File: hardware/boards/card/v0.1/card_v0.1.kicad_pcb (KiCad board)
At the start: 6 copper layers, 67.6 x 25.4 mm, 63 parts, among them IC1 IS42S16160J-7BLI, IC2 IS42S16160J-7BLI, J1 SODIMM-200, J2 USB_HOST, J3 USB_DEVICE, J4 SD_CARD, J5 DEBUG, J6 SPI, J7 UART4, J8 Conn_01x16_Pin, J9 AUDIO_IN, U1 CS42528K-CQZ, U2 STM32H747XIHx, U3 NJM4580E-TE1, U4 NJM4580E-TE1, Y1 Crystal, Y2 Crystal

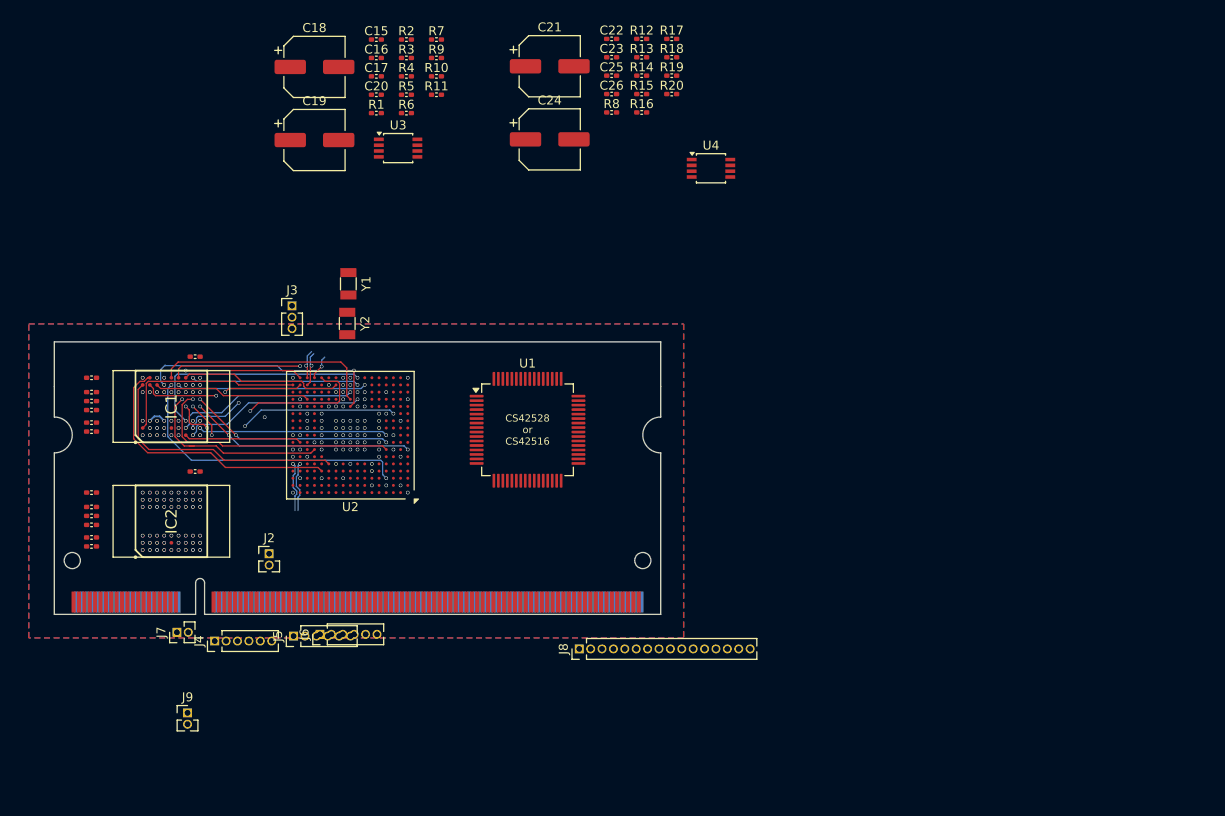
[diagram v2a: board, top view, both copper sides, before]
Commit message: boards/card: route audio input channels and 4 output channel buffers
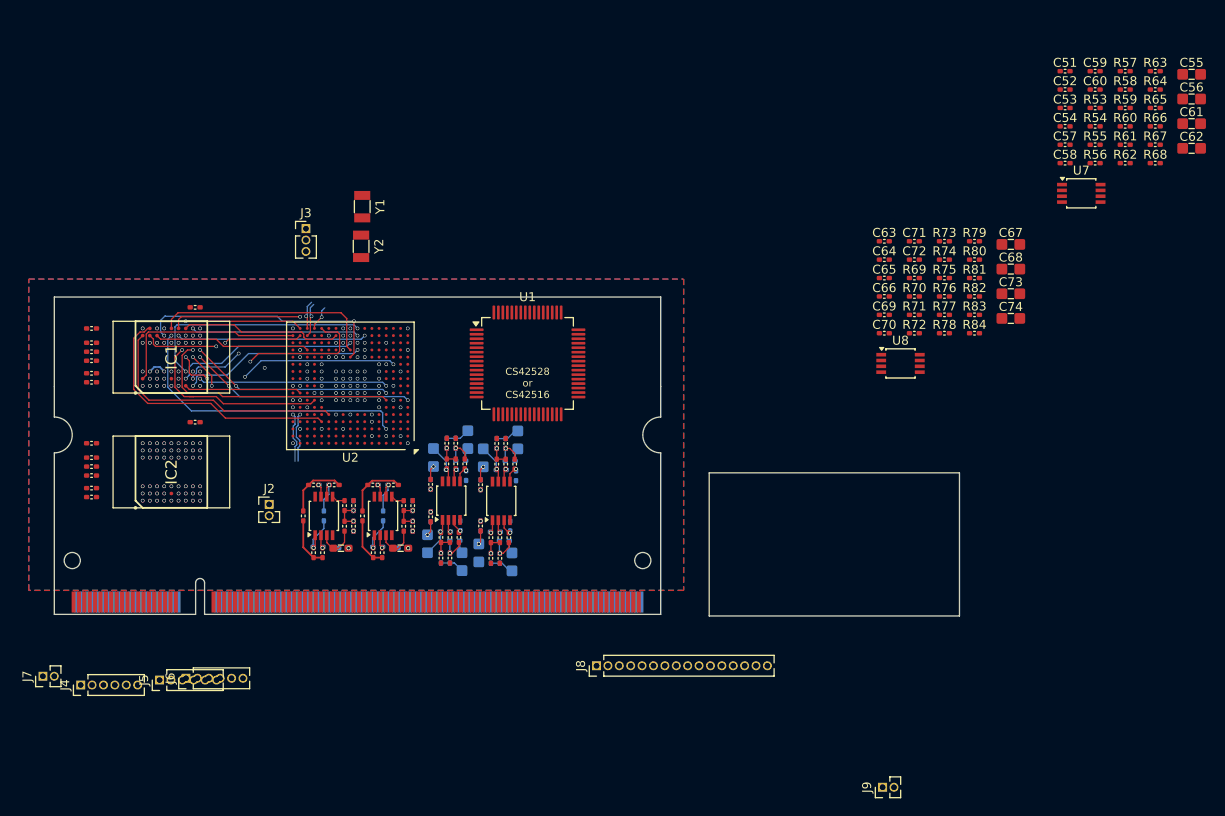
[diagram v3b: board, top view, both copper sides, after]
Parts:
- added C27: 2n2 FILM, rhais_rcl.pretty-main:C0603, F.Cu at (88.5, 69.0)
- added C28: 2n2 FILM, rhais_rcl.pretty-main:C0603, F.Cu at (81.8, 69.0)
- added C29: 4.7uF X7R, rhais_rcl.pretty-main:C0402, B.Cu at (83.2, 66.5)
- added C30: 47uF X5R, rhais_rcl.pretty-main:C0805, B.Cu at (95.3, 70.5)
- added C31: 1n2 C0G, rhais_rcl.pretty-main:C0402, B.Cu at (95.1, 66.5)
- added C32: 47uF X5R, rhais_rcl.pretty-main:C0805, B.Cu at (91.5, 68.5)
- added C33: 1n8 C0G, rhais_rcl.pretty-main:C0402, B.Cu at (93.6, 57.3)
- added C34: 5n8 C0G, rhais_rcl.pretty-main:C0402, B.Cu at (94.6, 57.3)
- added C35: 47uF X5R, rhais_rcl.pretty-main:C0805, B.Cu at (96.0, 56.9)
- added C36: 1n2 C0G, rhais_rcl.pretty-main:C0402, B.Cu at (95.8, 60.9)
- added C37: 390pF C0G, rhais_rcl.pretty-main:C0402, B.Cu at (94.1, 60.2)
- added C38: 47uF X5R, rhais_rcl.pretty-main:C0805, B.Cu at (92.1, 58.9)
- added C39: 1n8 C0G, rhais_rcl.pretty-main:C0402, B.Cu at (98.5, 70.1)
- added C40: 5n8 C0G, rhais_rcl.pretty-main:C0402, B.Cu at (99.5, 70.1)
- added C41: 1n8 C0G, rhais_rcl.pretty-main:C0402, B.Cu at (99.2, 57.3)
- added C42: 5n8 C0G, rhais_rcl.pretty-main:C0402, B.Cu at (100.2, 57.3)
- added C43: 47uF X5R, rhais_rcl.pretty-main:C0805, B.Cu at (100.9, 70.5)
- added C44: 47uF X5R, rhais_rcl.pretty-main:C0805, B.Cu at (101.5, 56.9)
- added C45: 1n2 C0G, rhais_rcl.pretty-main:C0402, B.Cu at (100.7, 66.5)
- added C46: 1n2 C0G, rhais_rcl.pretty-main:C0402, B.Cu at (101.3, 60.9)
- added C47: 390pF C0G, rhais_rcl.pretty-main:C0402, B.Cu at (99.0, 67.2)
- added C48: 390pF C0G, rhais_rcl.pretty-main:C0402, B.Cu at (99.7, 60.3)
- added C49: 47uF X5R, rhais_rcl.pretty-main:C0805, B.Cu at (97.2, 69.5)
- added C50: 47uF X5R, rhais_rcl.pretty-main:C0805, B.Cu at (97.7, 58.9)
- added C51: 1n8 C0G, rhais_rcl.pretty-main:C0402, F.Cu at (162.5, 15.8)
- added C52: 5n8 C0G, rhais_rcl.pretty-main:C0402, F.Cu at (162.5, 17.9)
- added C53: 1n8 C0G, rhais_rcl.pretty-main:C0402, F.Cu at (162.5, 19.9)
- added C54: 5n8 C0G, rhais_rcl.pretty-main:C0402, F.Cu at (162.5, 22.0)
- added C55: 47uF X5R, rhais_rcl.pretty-main:C0805, F.Cu at (176.6, 16.2)
- added C56: 47uF X5R, rhais_rcl.pretty-main:C0805, F.Cu at (176.6, 18.9)
- added C57: 1n2 C0G, rhais_rcl.pretty-main:C0402, F.Cu at (162.5, 24.0)
- added C58: 1n2 C0G, rhais_rcl.pretty-main:C0402, F.Cu at (162.5, 26.1)
- added C59: 390pF C0G, rhais_rcl.pretty-main:C0402, F.Cu at (165.9, 15.8)
- added C60: 390pF C0G, rhais_rcl.pretty-main:C0402, F.Cu at (165.9, 17.9)
- added C61: 47uF X5R, rhais_rcl.pretty-main:C0805, F.Cu at (176.6, 21.7)
- added C62: 47uF X5R, rhais_rcl.pretty-main:C0805, F.Cu at (176.6, 24.4)
- added C63: 1n8 C0G, rhais_rcl.pretty-main:C0402, F.Cu at (142.4, 34.8)
- added C64: 5n8 C0G, rhais_rcl.pretty-main:C0402, F.Cu at (142.4, 36.8)
- added C65: 1n8 C0G, rhais_rcl.pretty-main:C0402, F.Cu at (142.4, 38.9)
- added C66: 5n8 C0G, rhais_rcl.pretty-main:C0402, F.Cu at (142.4, 40.9)
- added C67: 47uF X5R, rhais_rcl.pretty-main:C0805, F.Cu at (156.5, 35.1)
- added C68: 47uF X5R, rhais_rcl.pretty-main:C0805, F.Cu at (156.5, 37.9)
- added C69: 1n2 C0G, rhais_rcl.pretty-main:C0402, F.Cu at (142.4, 43.0)
- added C70: 1n2 C0G, rhais_rcl.pretty-main:C0402, F.Cu at (142.4, 45.0)
- added C71: 390pF C0G, rhais_rcl.pretty-main:C0402, F.Cu at (145.7, 34.8)
- added C72: 390pF C0G, rhais_rcl.pretty-main:C0402, F.Cu at (145.7, 36.8)
- added C73: 47uF X5R, rhais_rcl.pretty-main:C0805, F.Cu at (156.5, 40.6)
- added C74: 47uF X5R, rhais_rcl.pretty-main:C0805, F.Cu at (156.5, 43.4)
- added R21: 2k94, rhais_rcl.pretty-main:R0402, F.Cu at (94.0, 67.8)
- added R22: 5k49, rhais_rcl.pretty-main:R0402, F.Cu at (93.0, 70.1)
- added R23: 1k65, rhais_rcl.pretty-main:R0402, F.Cu at (94.0, 70.1)
- added R24: 887R, rhais_rcl.pretty-main:R0402, F.Cu at (95.0, 67.8)
- added R25: 6k19, rhais_rcl.pretty-main:R0402, F.Cu at (93.0, 67.8)
- added R26: 1k87, rhais_rcl.pretty-main:R0402, B.Cu at (94.5, 68.2)
- added R27: 1k, rhais_rcl.pretty-main:R0402, F.Cu at (91.8, 65.5)
- added R28: 47k5, rhais_rcl.pretty-main:R0402, B.Cu at (91.8, 65.5)
- added R29: 5k49, rhais_rcl.pretty-main:R0402, F.Cu at (93.6, 57.3)
- added R30: 1k65, rhais_rcl.pretty-main:R0402, F.Cu at (94.6, 57.3)
- added R31: 6k19, rhais_rcl.pretty-main:R0402, F.Cu at (93.6, 59.6)
- added R32: 2k94, rhais_rcl.pretty-main:R0402, F.Cu at (94.6, 59.6)
- added R33: 887R, rhais_rcl.pretty-main:R0402, F.Cu at (95.6, 59.6)
- added R34: 1k87, rhais_rcl.pretty-main:R0402, B.Cu at (95.2, 59.2)
- added R35: 1k, rhais_rcl.pretty-main:R0402, F.Cu at (91.8, 61.9)
- added R36: 47k5, rhais_rcl.pretty-main:R0402, B.Cu at (91.8, 61.9)
- added R37: 5k49, rhais_rcl.pretty-main:R0402, F.Cu at (98.5, 70.1)
- added R38: 1k65, rhais_rcl.pretty-main:R0402, F.Cu at (99.5, 70.1)
- added R39: 5k49, rhais_rcl.pretty-main:R0402, F.Cu at (99.2, 57.3)
- added R40: 1k65, rhais_rcl.pretty-main:R0402, F.Cu at (100.2, 57.3)
- added R41: 6k19, rhais_rcl.pretty-main:R0402, F.Cu at (98.5, 67.8)
- added R42: 2k94, rhais_rcl.pretty-main:R0402, F.Cu at (99.5, 67.8)
- added R43: 887R, rhais_rcl.pretty-main:R0402, F.Cu at (100.5, 67.8)
- added R44: 1k87, rhais_rcl.pretty-main:R0402, B.Cu at (100.0, 68.2)
- added R45: 6k19, rhais_rcl.pretty-main:R0402, F.Cu at (99.2, 59.6)
- added R46: 2k94, rhais_rcl.pretty-main:R0402, F.Cu at (100.2, 59.6)
- added R47: 887R, rhais_rcl.pretty-main:R0402, F.Cu at (101.2, 59.6)
- added R48: 1k87, rhais_rcl.pretty-main:R0402, B.Cu at (100.7, 59.3)
- added R49: 1k, rhais_rcl.pretty-main:R0402, F.Cu at (97.4, 66.5)
- added R50: 1k, rhais_rcl.pretty-main:R0402, F.Cu at (97.4, 61.9)
- added R51: 47k5, rhais_rcl.pretty-main:R0402, B.Cu at (97.4, 66.5)
- added R52: 47k5, rhais_rcl.pretty-main:R0402, B.Cu at (97.4, 61.9)
- added R53: 5k49, rhais_rcl.pretty-main:R0402, F.Cu at (165.9, 19.9)
- added R54: 1k65, rhais_rcl.pretty-main:R0402, F.Cu at (165.9, 22.0)
- added R55: 5k49, rhais_rcl.pretty-main:R0402, F.Cu at (165.9, 24.0)
- added R56: 1k65, rhais_rcl.pretty-main:R0402, F.Cu at (165.9, 26.1)
- added R57: 6k19, rhais_rcl.pretty-main:R0402, F.Cu at (169.2, 15.8)
- added R58: 2k94, rhais_rcl.pretty-main:R0402, F.Cu at (169.2, 17.9)
- added R59: 887R, rhais_rcl.pretty-main:R0402, F.Cu at (169.2, 19.9)
- added R60: 1k87, rhais_rcl.pretty-main:R0402, F.Cu at (169.2, 22.0)
- added R61: 6k19, rhais_rcl.pretty-main:R0402, F.Cu at (169.2, 24.0)
- added R62: 2k94, rhais_rcl.pretty-main:R0402, F.Cu at (169.2, 26.1)
- added R63: 887R, rhais_rcl.pretty-main:R0402, F.Cu at (172.6, 15.8)
- added R64: 1k87, rhais_rcl.pretty-main:R0402, F.Cu at (172.6, 17.9)
- added R65: 1k, rhais_rcl.pretty-main:R0402, F.Cu at (172.6, 19.9)
- added R66: 1k, rhais_rcl.pretty-main:R0402, F.Cu at (172.6, 22.0)
- added R67: 47k5, rhais_rcl.pretty-main:R0402, F.Cu at (172.6, 24.0)
- added R68: 47k5, rhais_rcl.pretty-main:R0402, F.Cu at (172.6, 26.1)
- added R69: 5k49, rhais_rcl.pretty-main:R0402, F.Cu at (145.7, 38.9)
- added R70: 1k65, rhais_rcl.pretty-main:R0402, F.Cu at (145.7, 40.9)
- added R71: 5k49, rhais_rcl.pretty-main:R0402, F.Cu at (145.7, 43.0)
- added R72: 1k65, rhais_rcl.pretty-main:R0402, F.Cu at (145.7, 45.0)
- added R73: 6k19, rhais_rcl.pretty-main:R0402, F.Cu at (149.1, 34.8)
- added R74: 2k94, rhais_rcl.pretty-main:R0402, F.Cu at (149.1, 36.8)
- added R75: 887R, rhais_rcl.pretty-main:R0402, F.Cu at (149.1, 38.9)
- added R76: 1k87, rhais_rcl.pretty-main:R0402, F.Cu at (149.1, 40.9)
- added R77: 6k19, rhais_rcl.pretty-main:R0402, F.Cu at (149.1, 43.0)
- added R78: 2k94, rhais_rcl.pretty-main:R0402, F.Cu at (149.1, 45.0)
- added R79: 887R, rhais_rcl.pretty-main:R0402, F.Cu at (152.4, 34.8)
- added R80: 1k87, rhais_rcl.pretty-main:R0402, F.Cu at (152.4, 36.8)
- added R81: 1k, rhais_rcl.pretty-main:R0402, F.Cu at (152.4, 38.9)
- added R82: 1k, rhais_rcl.pretty-main:R0402, F.Cu at (152.4, 40.9)
- added R83: 47k5, rhais_rcl.pretty-main:R0402, F.Cu at (152.4, 43.0)
- added R84: 47k5, rhais_rcl.pretty-main:R0402, F.Cu at (152.4, 45.0)
- added U5: NJM4580E-TE1, Package_SO:TSSOP-8_3x3mm_P0.65mm, F.Cu at (94.1, 63.7)
- added U6: NJM4580E-TE1, Package_SO:TSSOP-8_3x3mm_P0.65mm, F.Cu at (99.7, 63.7)
- added U7: NJM4580E-TE1, Package_SO:TSSOP-8_3x3mm_P0.65mm, F.Cu at (164.3, 29.4)
- added U8: NJM4580E-TE1, Package_SO:TSSOP-8_3x3mm_P0.65mm, F.Cu at (144.2, 48.4)
- C15, C26: value 2700pF C0G -> 2n7 C0G
- C16, C17, C20, C22, C23, C25, R17, R3: moved to B.Cu
- C18: value 100uF ELEC -> 1n8 C0G; footprint Capacitor_SMD:CP_Elec_6.3x5.7 -> rhais_rcl.pretty-main:C0402; moved to B.Cu
- C19: value 100uF ELEC -> 5n8 C0G; footprint Capacitor_SMD:CP_Elec_6.3x5.7 -> rhais_rcl.pretty-main:C0402; moved to B.Cu
- C21: value 100uF ELEC -> 4.7uF X7R; footprint Capacitor_SMD:CP_Elec_6.3x5.7 -> rhais_rcl.pretty-main:C0402; moved to B.Cu
- C24: value 100uF ELEC -> 390pF C0G; footprint Capacitor_SMD:CP_Elec_6.3x5.7 -> rhais_rcl.pretty-main:C0402; moved to B.Cu
- R11, R12: value 100k -> 10k; moved to B.Cu
- moved J9 77.9 mm to (142.2, 95.7), turned to 90 degrees
- moved R18 68.1 mm to (78.8, 69.5), turned to -90 degrees
- moved R17 65.8 mm to (79.9, 65.4), turned to 90 degrees
- moved R12 65.8 mm to (82.1, 69.0), turned to 180 degrees
- moved C23 63.6 mm to (79.2, 68.8), turned to 180 degrees
- moved R15 62.3 mm to (79.8, 69.5), turned to -90 degrees
- moved R14 59.6 mm to (83.2, 66.5), turned to -90 degrees
- moved C22 59.5 mm to (83.2, 64.2), turned to 90 degrees
- moved R13 59.4 mm to (83.2, 64.2), turned to -90 degrees
- moved R19 59.1 mm to (81.0, 62.0)
- moved R20 59.1 mm to (78.8, 62.0), turned to 180 degrees
- moved C26 58.2 mm to (77.6, 65.4), turned to 90 degrees
- moved U4 58.0 mm to (79.9, 65.4), turned to 90 degrees
- moved C18 56.5 mm to (93.0, 70.1), turned to 90 degrees
- moved C25 55.8 mm to (79.9, 62.0), turned to 180 degrees
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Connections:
- C16 pad 1: Net-(U3B-+) -> Net-(U3B--)
- C17 pad 1: Net-(U3A-+) -> Net-(U3A--)
- C18 pad 1: Net-(U3A-+) -> GND
- C18 pad 2: /IN_L -> Net-(C18-Pad2)
- C19 pad 1: Net-(C19-Pad1) -> GND
- C19 pad 2: GND -> Net-(C19-Pad2)
- C20 pad 1: Net-(C19-Pad1) -> Net-(C20-Pad1)
- C21 pad 1: Net-(U4A-+) -> Net-(C20-Pad1)
- C21 pad 2: /IN_R -> GND
- C23 pad 1: Net-(U4A-+) -> Net-(U4A--)
- C24 pad 1: Net-(C22-Pad1) -> Net-(U5A--)
- C24 pad 2: GND -> Net-(C24-Pad2)
- C25 pad 1: Net-(U4B-+) -> Net-(U4B--)
- J8 pad 1: Net-(J8-Pin_1) -> /OUT_B4
- J8 pad 10: Net-(J8-Pin_10) -> /OUT_B1
- J8 pad 11: Net-(J8-Pin_11) -> /OUT_A1
- J8 pad 12: Net-(J8-Pin_12) -> unconnected-(J8-Pin_12-Pad12)
- J8 pad 13: Net-(J8-Pin_13) -> unconnected-(J8-Pin_13-Pad13)
- J8 pad 14: Net-(J8-Pin_14) -> unconnected-(J8-Pin_14-Pad14)
- J8 pad 15: Net-(J8-Pin_15) -> unconnected-(J8-Pin_15-Pad15)
- J8 pad 16: Net-(J8-Pin_16) -> unconnected-(J8-Pin_16-Pad16)
- J8 pad 2: Net-(J8-Pin_2) -> /OUT_A4
- J8 pad 3: Net-(J8-Pin_3) -> unconnected-(J8-Pin_3-Pad3)
- J8 pad 4: Net-(J8-Pin_4) -> /OUT_B3
- J8 pad 5: Net-(J8-Pin_5) -> /OUT_A3
- J8 pad 6: Net-(J8-Pin_6) -> unconnected-(J8-Pin_6-Pad6)
- J8 pad 7: Net-(J8-Pin_7) -> /OUT_B2
- J8 pad 8: Net-(J8-Pin_8) -> /OUT_A2
- J8 pad 9: Net-(J8-Pin_9) -> unconnected-(J8-Pin_9-Pad9)
- R10 pad 1: Net-(C19-Pad1) -> Net-(C20-Pad1)
- R15 pad 1: Net-(U4A-+) -> Net-(U4A--)
- R16 pad 2: Net-(U4B--) -> Net-(U4B-+)
- R17 pad 2: Net-(U4B-+) -> Net-(U4B--)
- R19 pad 1: Net-(U4B-+) -> Net-(U4B--)
- R2 pad 1: Net-(U3B-+) -> Net-(U3B--)
- R3 pad 2: Net-(U3B-+) -> Net-(U3B--)
- R5 pad 1: Net-(U3A-+) -> Net-(U3A--)
- R6 pad 1: Net-(C19-Pad1) -> Net-(C20-Pad1)
- R6 pad 2: Net-(U3B--) -> Net-(U3B-+)
- R7 pad 1: Net-(C19-Pad1) -> Net-(C20-Pad1)
- R7 pad 2: Net-(U3A--) -> Net-(U3A-+)
- R8 pad 2: Net-(U4A--) -> Net-(U4A-+)
- R9 pad 2: Net-(C19-Pad1) -> Net-(C20-Pad1)
- U1 pad 20: Net-(J8-Pin_1) -> /AOUTB4-
- U1 pad 21: Net-(J8-Pin_2) -> /AOUTB4+
- U1 pad 22: Net-(J8-Pin_4) -> /AOUTA4+
- U1 pad 23: Net-(J8-Pin_3) -> /AOUTA4-
- U1 pad 26: Net-(J8-Pin_5) -> /AOUTB3-
- U1 pad 27: Net-(J8-Pin_6) -> /AOUTB3+
- U1 pad 28: Net-(J8-Pin_8) -> /AOUTA3+
- U1 pad 29: Net-(J8-Pin_7) -> /AOUTA3-
- U1 pad 30: Net-(J8-Pin_9) -> /AOUTB2-
- U1 pad 31: Net-(J8-Pin_10) -> /AOUTB2+
- U1 pad 32: Net-(J8-Pin_12) -> /AOUTA2+
- U1 pad 33: Net-(J8-Pin_11) -> /AOUTA2-
- U1 pad 34: Net-(J8-Pin_13) -> /AOUTB1-
- U1 pad 35: Net-(J8-Pin_14) -> /AOUTB1+
- U1 pad 36: Net-(J8-Pin_16) -> /AOUTA1+
- U1 pad 37: Net-(J8-Pin_15) -> /AOUTA1-
- U3 pad 4: unconnected-(U3C-V--Pad4) -> GND
- U3 pad 8: unconnected-(U3C-V+-Pad8) -> +5V
- U4 pad 4: (no net) -> +5V
- U4 pad 8: (no net) -> GND
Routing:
- net GND: track 0.00 -> 11.1 mm, vias 61 -> 63
- net /AINR-: track 0.00 -> 6.96 mm
- net /AINL-: track 0.00 -> 6.94 mm
- net /AINL+: track 0.00 -> 5.60 mm
- net /AINR+: track 0.00 -> 5.58 mm
- net Net-(C23-Pad2): track 0.00 -> 4.87 mm, vias 0 -> 1
- net Net-(C17-Pad2): track 0.00 -> 4.83 mm, vias 0 -> 1
- net Net-(U3A-+): track 0.00 -> 4.64 mm
- net Net-(U4A-+): track 0.00 -> 4.62 mm
- net Net-(U4B--): track 0.00 -> 4.54 mm, vias 0 -> 1
- net Net-(U3B--): track 0.00 -> 4.54 mm, vias 0 -> 1
- net Net-(C37-Pad2): track 0.00 -> 4.42 mm, vias 0 -> 1
- net Net-(C48-Pad2): track 0.00 -> 4.42 mm, vias 0 -> 1
- net Net-(C24-Pad2): track 0.00 -> 4.42 mm, vias 0 -> 1
- net Net-(C34-Pad2): track 0.00 -> 3.31 mm, vias 0 -> 1
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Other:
- board size 67.6 x 25.4 mm -> 100.9 x 35.5 mm

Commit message: card: route remaining 2 codec output stages
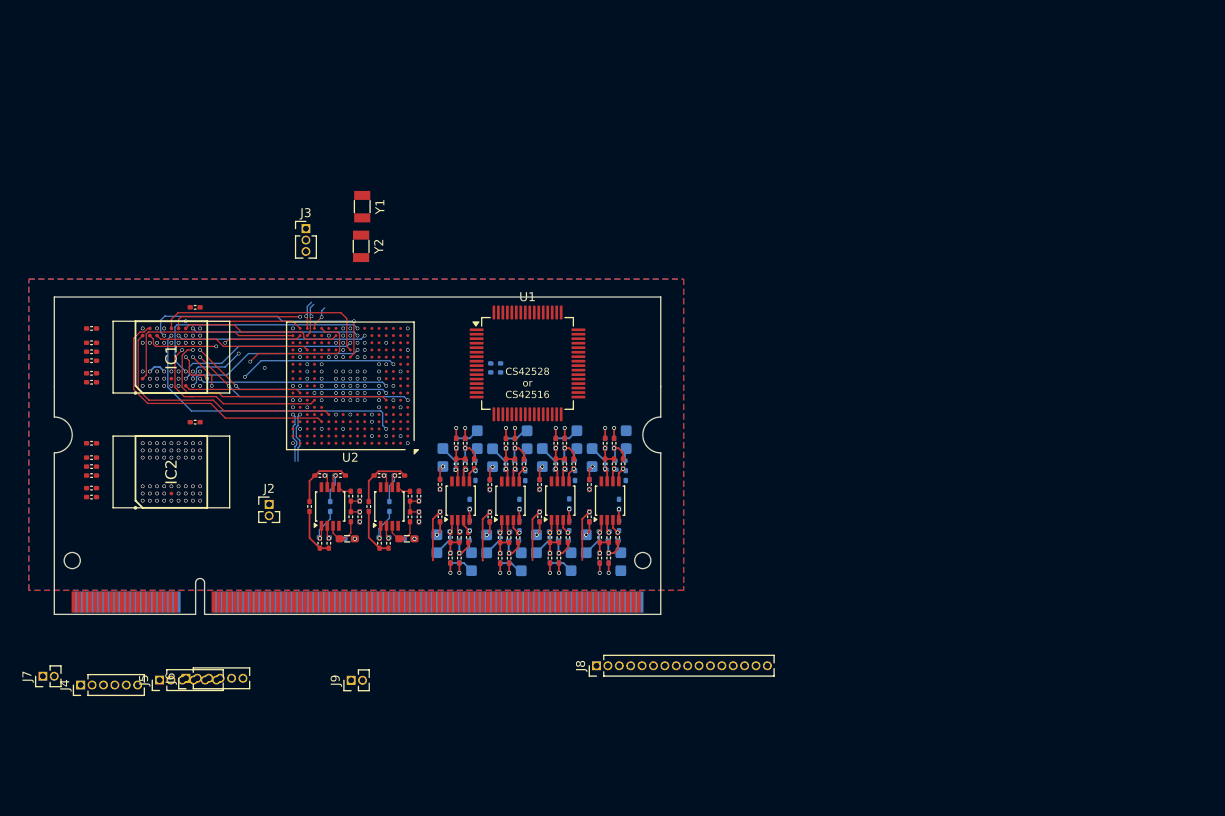
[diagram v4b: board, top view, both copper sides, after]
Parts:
- added C75: 100nF X5R, rhais_rcl.pretty-main:C0402, B.Cu at (112.8, 64.1)
- added C76: 100nF X5R, rhais_rcl.pretty-main:C0402, B.Cu at (107.2, 64.0)
- added C77: 100nF X5R, rhais_rcl.pretty-main:C0402, B.Cu at (101.7, 64.1)
- added C78: 100nF X5R, rhais_rcl.pretty-main:C0402, B.Cu at (96.2, 64.1)
- added R85: 10k, rhais_rcl.pretty-main:R0402, B.Cu at (99.0, 49.4)
- added R86: 10k, rhais_rcl.pretty-main:R0402, B.Cu at (99.0, 48.4)
- C51, C52, C53, C54, C55, C56, C57, C58, C59, C60, C61, C62, C63, C64, C65, C66, C67, C68, C69, C70, C71, C72, C73, C74, R60, R64, R67, R68, R76, R80, R83, R84: moved to B.Cu
- moved C55 88.0 mm to (107.5, 70.5), turned to -90 degrees
- moved C61 86.7 mm to (103.6, 68.5), turned to 90 degrees
- moved R57 82.5 mm to (105.1, 67.8), turned to 90 degrees
- moved R65 82.4 mm to (104.0, 65.5), turned to 90 degrees
- moved R58 80.5 mm to (106.1, 67.8), turned to 90 degrees
- moved R67 80.2 mm to (104.0, 65.5), turned to 90 degrees
- moved C62 80.2 mm to (104.2, 58.9), turned to -90 degrees
- moved R66 79.4 mm to (104.0, 61.9), turned to -90 degrees
- moved C59 79.2 mm to (105.6, 67.2), turned to 180 degrees
- moved C51 79.0 mm to (105.1, 70.1), turned to 90 degrees
- moved R53 78.8 mm to (105.1, 70.1), turned to 90 degrees
- moved R59 78.4 mm to (107.1, 67.8), turned to 90 degrees
- moved C56 78.3 mm to (108.1, 56.9), turned to 90 degrees
- moved R63 78.2 mm to (107.8, 59.6), turned to -90 degrees
- moved R60 77.8 mm to (106.6, 68.2)
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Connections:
- U1 pad 10: unconnected-(U1-AD0/CS-Pad10) -> Net-(U1-AD0/CS)
- U1 pad 9: unconnected-(U1-AD1/CDIN-Pad9) -> Net-(U1-AD1/CDIN)
- U5 pad 4: (no net) -> +5V
- U5 pad 8: (no net) -> GND
- U6 pad 4: (no net) -> +5V
- U6 pad 8: (no net) -> GND
- U7 pad 4: (no net) -> +5V
- U7 pad 8: (no net) -> GND
- U8 pad 4: (no net) -> +5V
- U8 pad 8: (no net) -> GND
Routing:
- net /AOUTB4-: track 0.00 -> 10.9 mm, vias 0 -> 1
- net /AOUTB1-: track 0.00 -> 10.9 mm, vias 0 -> 1
- net /AOUTB2-: track 0.00 -> 10.9 mm, vias 0 -> 1
- net /AOUTB4+: track 0.00 -> 10.9 mm, vias 0 -> 1
- net /AOUTB1+: track 0.00 -> 10.9 mm, vias 0 -> 1
- net /AOUTB3-: track 0.00 -> 10.8 mm, vias 0 -> 1
- net /AOUTB2+: track 0.00 -> 10.8 mm, vias 0 -> 1
- net /AOUTB3+: track 0.00 -> 10.8 mm, vias 0 -> 1
- net /OUT_A4: track 0.00 -> 8.25 mm
- net /OUT_A3: track 0.00 -> 8.24 mm
- net /OUT_A2: track 0.00 -> 8.23 mm, vias 0 -> 1
- net /OUT_A1: track 0.00 -> 8.23 mm, vias 0 -> 1
- net /OUT_B3: track 0.00 -> 5.74 mm
- net /OUT_B4: track 0.00 -> 5.73 mm
- net /OUT_B2: track 0.00 -> 5.73 mm, vias 0 -> 1
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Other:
- board size 100.9 x 35.5 mm -> 67.6 x 30.3 mm
- board text removed: "TODO: may need to change codec due to ELECs"

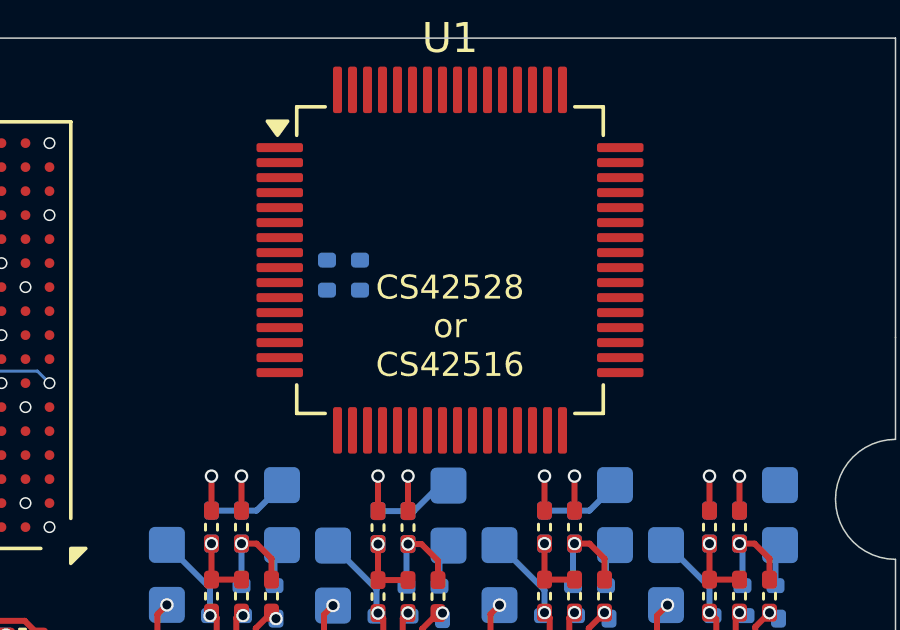
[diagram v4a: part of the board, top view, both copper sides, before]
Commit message: card: add filter caps for codec
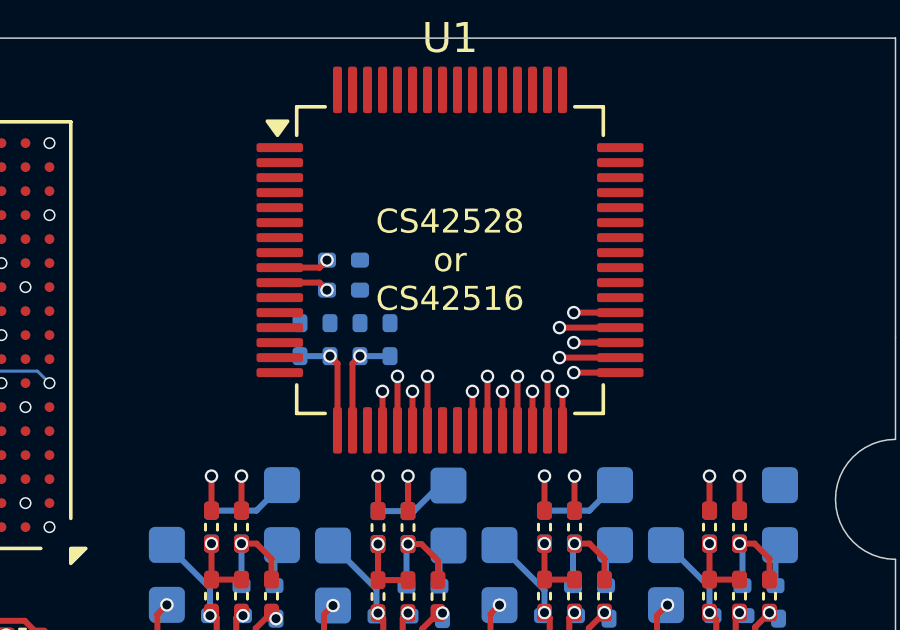
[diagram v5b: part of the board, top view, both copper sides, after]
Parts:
- added C81: 0.1uF, rhais_rcl.pretty-main:C0402, B.Cu at (98.6, 51.0)
- added C82: 4.7uF, rhais_rcl.pretty-main:C0402, B.Cu at (97.6, 51.0)
- added C83: 0.1uF, rhais_rcl.pretty-main:C0402, B.Cu at (99.6, 51.0)
- added C84: 100uF, rhais_rcl.pretty-main:C0402, B.Cu at (100.6, 51.0)
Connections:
- net /AINL+ renamed /Audio Codec/AINL+
- net /AINL- renamed /Audio Codec/AINL-
- net /AINR+ renamed /Audio Codec/AINR+
- net /AINR- renamed /Audio Codec/AINR-
- net /AOUTA1+ renamed /Audio Codec/AOUTA1+
- net /AOUTA1- renamed /Audio Codec/AOUTA1-
- net /AOUTA2+ renamed /Audio Codec/AOUTA2+
- net /AOUTA2- renamed /Audio Codec/AOUTA2-
- net /AOUTA3+ renamed /Audio Codec/AOUTA3+
- net /AOUTA3- renamed /Audio Codec/AOUTA3-
- net /AOUTA4+ renamed /Audio Codec/AOUTA4+
- net /AOUTA4- renamed /Audio Codec/AOUTA4-
- net /AOUTB1+ renamed /Audio Codec/AOUTB1+
- net /AOUTB1- renamed /Audio Codec/AOUTB1-
- net /AOUTB2+ renamed /Audio Codec/AOUTB2+
- net /AOUTB2- renamed /Audio Codec/AOUTB2-
- net /AOUTB3+ renamed /Audio Codec/AOUTB3+
- net /AOUTB3- renamed /Audio Codec/AOUTB3-
- net /AOUTB4+ renamed /Audio Codec/AOUTB4+
- net /AOUTB4- renamed /Audio Codec/AOUTB4-
- net /IN_L renamed /Audio Codec/IN_L
- net /IN_R renamed /Audio Codec/IN_R
- net /OUT_A1 renamed /Audio Codec/OUT_A1
- net /OUT_A2 renamed /Audio Codec/OUT_A2
- net /OUT_A3 renamed /Audio Codec/OUT_A3
- net /OUT_A4 renamed /Audio Codec/OUT_A4
- net /OUT_B1 renamed /Audio Codec/OUT_B1
- net /OUT_B2 renamed /Audio Codec/OUT_B2
- net /OUT_B3 renamed /Audio Codec/OUT_B3
- net /OUT_B4 renamed /Audio Codec/OUT_B4
- U1 pad 1: /SAI2_SD_A -> /Audio Codec/SAI2_SD_A
- U1 pad 17: unconnected-(U1-VQ-Pad17) -> Net-(U1-VQ)
- U1 pad 18: unconnected-(U1-FILT+-Pad18) -> Net-(U1-FILT+)
- U1 pad 2: /SAI1_SCK_A -> /Audio Codec/SAI1_SCK_A
- U1 pad 3: /SAI1_FS_A -> /Audio Codec/SAI1_FS_A
- U1 pad 39: unconnected-(U1-LPFLT-Pad39) -> Net-(U1-LPFLT)
- U1 pad 56: /SAI4_SD_B -> /Audio Codec/SAI4_SD_B
- U1 pad 59: /SAI1_MCLK_A -> /Audio Codec/SAI1_MCLK_A
- U1 pad 62: /SAI1_SD_B -> /Audio Codec/SAI1_SD_B
- U1 pad 63: /SAI1_SD_A -> /Audio Codec/SAI1_SD_A
- U1 pad 64: /SAI2_SD_B -> /Audio Codec/SAI2_SD_B
- U1 pad 7: /I2C2_SCL -> /Audio Codec/I2C2_SCL
- U1 pad 8: /I2C2_SDA -> /Audio Codec/I2C2_SDA
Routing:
- net Net-(U1-VQ): track 0.00 -> 3.58 mm, vias 0 -> 1
- net Net-(U1-FILT+): track 0.00 -> 3.58 mm, vias 0 -> 1
- net /Audio Codec/AOUTB1-: track 10.9 -> 12.9 mm, vias 1 -> 2
- net /Audio Codec/AOUTA1+: track 1.15 -> 3.18 mm, vias 1 -> 2
- net /Audio Codec/AOUTB4+: track 10.9 -> 12.7 mm, vias 1 -> 2
- net /Audio Codec/AOUTB3+: track 10.8 -> 12.6 mm, vias 1 -> 2
- net /Audio Codec/AOUTB2+: track 10.8 -> 12.6 mm, vias 1 -> 2
- net /Audio Codec/AOUTA4-: track 1.15 -> 2.95 mm, vias 1 -> 2
- net /Audio Codec/AOUTA3-: track 1.17 -> 2.97 mm, vias 1 -> 2
- net Net-(U1-AD1/CDIN): track 0.00 -> 1.68 mm, vias 0 -> 1
- net Net-(U1-AD0/CS): track 0.00 -> 1.68 mm, vias 0 -> 1
- net /Audio Codec/AOUTB1+: track 10.9 -> 12.4 mm, vias 1 -> 2
- net /Audio Codec/AOUTA2-: track 1.15 -> 2.70 mm, vias 1 -> 2
- net /Audio Codec/AOUTA1-: track 1.15 -> 2.70 mm, vias 1 -> 2
- net /Audio Codec/AOUTB4-: track 10.9 -> 12.2 mm, vias 1 -> 2
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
